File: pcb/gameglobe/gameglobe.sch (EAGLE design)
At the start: 16 parts

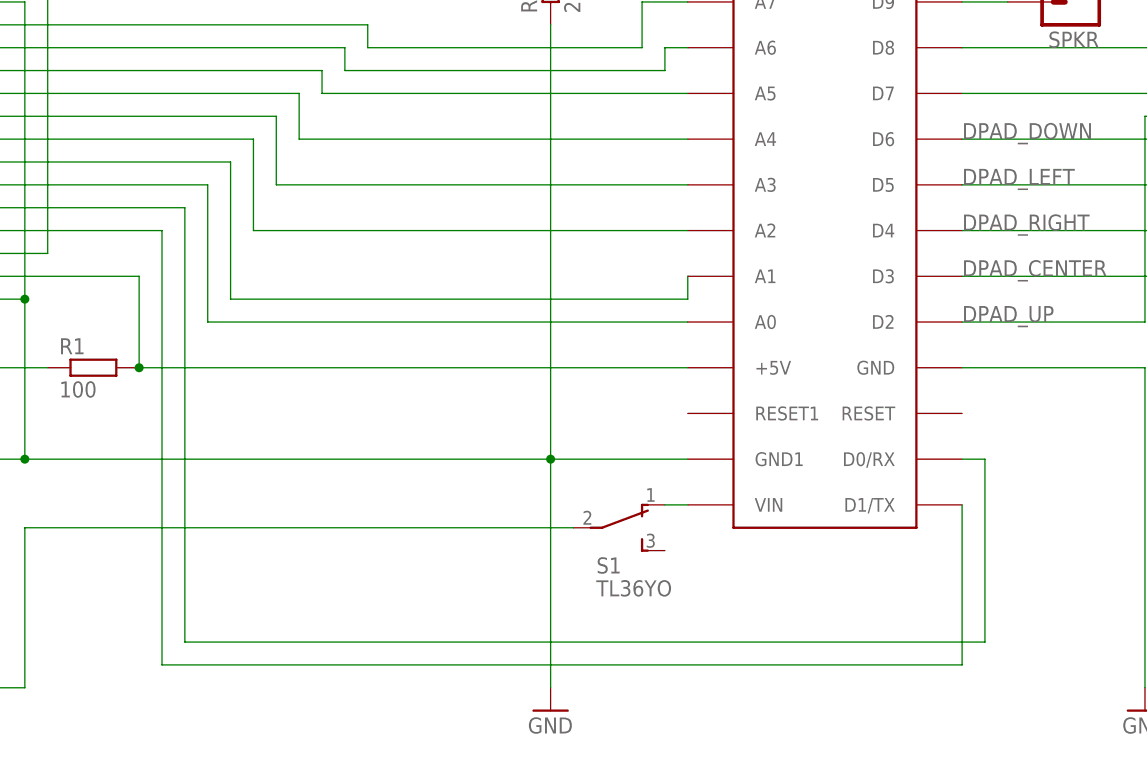
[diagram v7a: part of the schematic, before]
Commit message: Improved power plane layout, also improved silkscreen, updated mockup image with new pcb renders
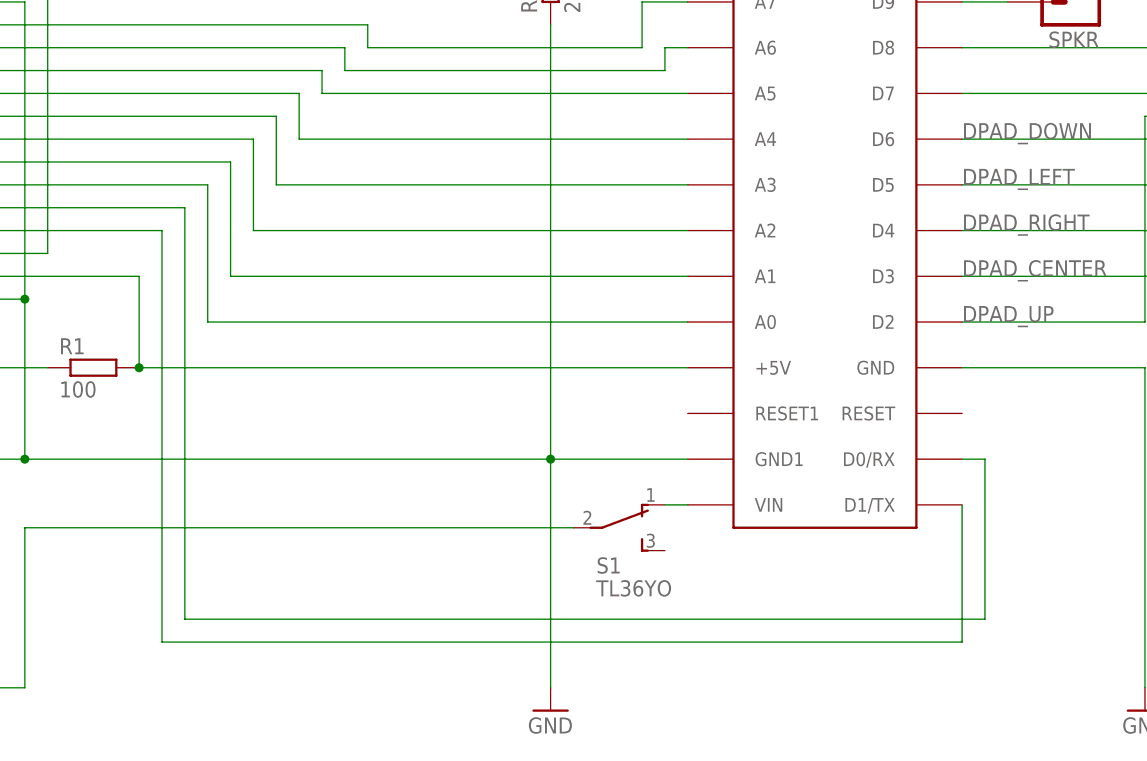
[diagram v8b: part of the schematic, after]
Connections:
- net N$11 renamed A0
- net N$12 renamed A1
- net N$13 renamed A2
- net N$14 renamed A3
- net N$15 renamed A4
- net N$16 renamed A5
- net N$17 renamed A6
- net N$18 renamed A7
- net N$7 renamed TX
- net N$8 renamed RX
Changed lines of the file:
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@@
 </segment>
 </net>
-<net name="N$7" class="0">
+<net name="TX" class="0">
 <segment>
 <pinref part="ARDUINO_NANO" gate="G$1" pin="D1/TX"/>
-<wire x1="132.08" y1="25.4" x2="132.08" y2="7.62" width="0.1524" layer="91"/>
-<wire x1="132.08" y1="7.62" x2="43.18" y2="7.62" width="0.1524" layer="91"/>
+<wire x1="132.08" y1="25.4" x2="132.08" y2="10.16" width="0.1524" layer="91"/>
+<wire x1="132.08" y1="10.16" x2="43.18" y2="10.16" width="0.1524" layer="91"/>
 <pinref part="JP2" gate="G$1" pin="4"/>
-<wire x1="43.18" y1="7.62" x2="43.18" y2="55.88" width="0.1524" layer="91"/>
+<wire x1="43.18" y1="10.16" x2="43.18" y2="55.88" width="0.1524" layer="91"/>
 <wire x1="43.18" y1="55.88" x2="22.86" y2="55.88" width="0.1524" layer="91"/>
 </segment>
 </net>
-<net name="N$8" class="0">
+<net name="RX" class="0">
 <segment>
 <pinref part="ARDUINO_NANO" gate="G$1" pin="D0/RX"/>
 <wire x1="132.08" y1="30.48" x2="134.62" y2="30.48" width="0.1524" layer="91"/>
-<wire x1="134.62" y1="30.48" x2="134.62" y2="10.16" width="0.1524" layer="91"/>
-<wire x1="134.62" y1="10.16" x2="45.72" y2="10.16" width="0.1524" layer="91"/>
+<wire x1="134.62" y1="30.48" x2="134.62" y2="12.7" width="0.1524" layer="91"/>
+<wire x1="134.62" y1="12.7" x2="45.72" y2="12.7" width="0.1524" layer="91"/>
 <pinref part="JP2" gate="G$1" pin="5"/>
-<wire x1="45.72" y1="10.16" x2="45.72" y2="58.42" width="0.1524" layer="91"/>
+<wire x1="45.72" y1="12.7" x2="45.72" y2="58.42" width="0.1524" layer="91"/>
 <wire x1="45.72" y1="58.42" x2="22.86" y2="58.42" width="0.1524" layer="91"/>
 </segment>
 </net>
-<net name="N$11" class="0">
+<net name="A0" class="0">
 <segment>
 <pinref part="ARDUINO_NANO" gate="G$1" pin="A0"/>
@@
 </segment>
 </net>
-<net name="N$12" class="0">
+<net name="A1" class="0">
 <segment>
 <pinref part="ARDUINO_NANO" gate="G$1" pin="A1"/>
-<wire x1="101.6" y1="50.8" x2="101.6" y2="48.26" width="0.1524" layer="91"/>
-<wire x1="101.6" y1="48.26" x2="50.8" y2="48.26" width="0.1524" layer="91"/>
-<wire x1="50.8" y1="48.26" x2="50.8" y2="63.5" width="0.1524" layer="91"/>
+<wire x1="101.6" y1="50.8" x2="50.8" y2="50.8" width="0.1524" layer="91"/>
+<wire x1="50.8" y1="50.8" x2="50.8" y2="63.5" width="0.1524" layer="91"/>
 <pinref part="JP2" gate="G$1" pin="7"/>
 <wire x1="50.8" y1="63.5" x2="22.86" y2="63.5" width="0.1524" layer="91"/>
 </segment>
 </net>
-<net name="N$13" class="0">
+<net name="A2" class="0">
 <segment>
 <pinref part="ARDUINO_NANO" gate="G$1" pin="A2"/>
@@
 </segment>
 </net>
-<net name="N$14" class="0">
+<net name="A3" class="0">
 <segment>
 <pinref part="ARDUINO_NANO" gate="G$1" pin="A3"/>
@@
 </segment>
 </net>
-<net name="N$15" class="0">
+<net name="A4" class="0">
 <segment>
 <pinref part="ARDUINO_NANO" gate="G$1" pin="A4"/>
@@
 </segment>
 </net>
-<net name="N$16" class="0">
+<net name="A5" class="0">
 <segment>
 <pinref part="ARDUINO_NANO" gate="G$1" pin="A5"/>
@@
 </segment>
 </net>
-<net name="N$17" class="0">
+<net name="A6" class="0">
 <segment>
 <pinref part="ARDUINO_NANO" gate="G$1" pin="A6"/>
@@
 </segment>
 </net>
-<net name="N$18" class="0">
+<net name="A7" class="0">
 <segment>
 <pinref part="ARDUINO_NANO" gate="G$1" pin="A7"/>
